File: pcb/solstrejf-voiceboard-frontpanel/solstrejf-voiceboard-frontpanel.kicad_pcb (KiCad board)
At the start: 2 copper layers, 41.1 x 123.4 mm, 14 parts, among them J1 Conn_02x08_Odd_Even, SW1 TRIG

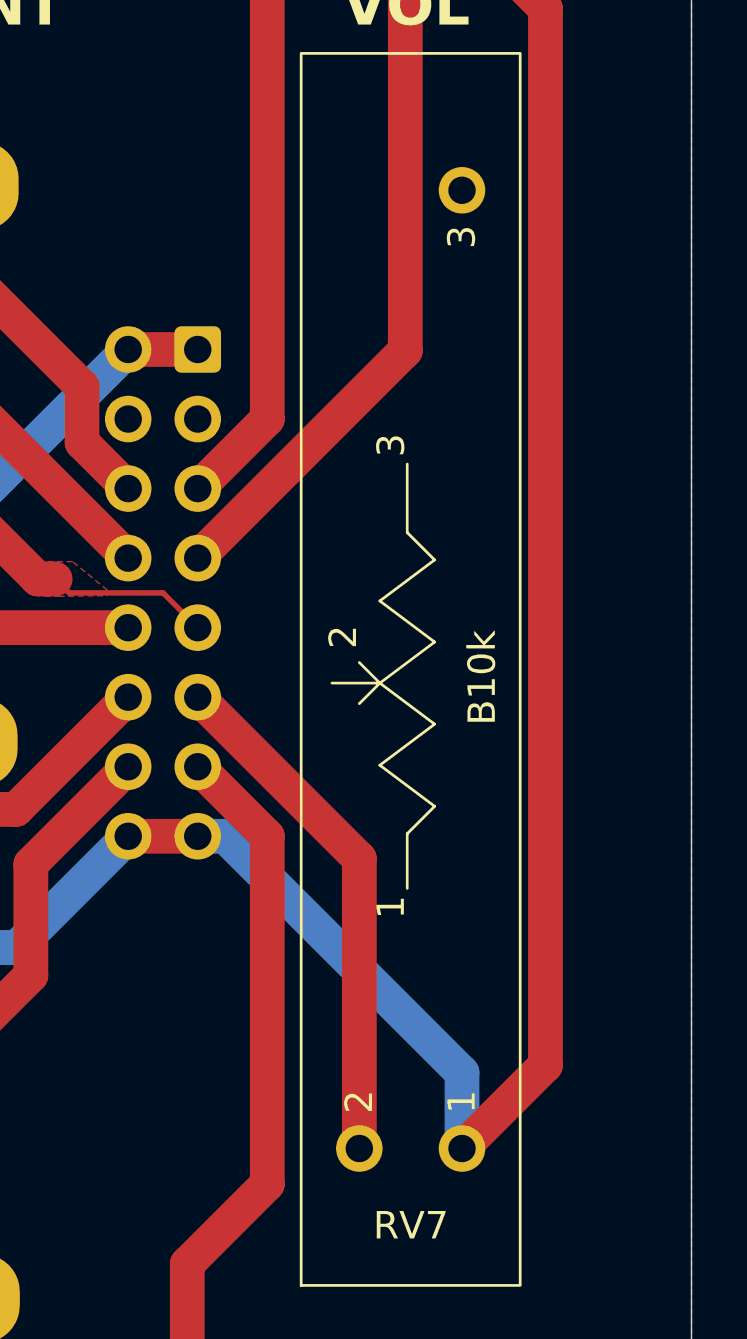
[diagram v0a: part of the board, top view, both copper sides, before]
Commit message: updated Alpha slide pot footprint to have 1.2mm drill hole diameter to match the 1mm pins
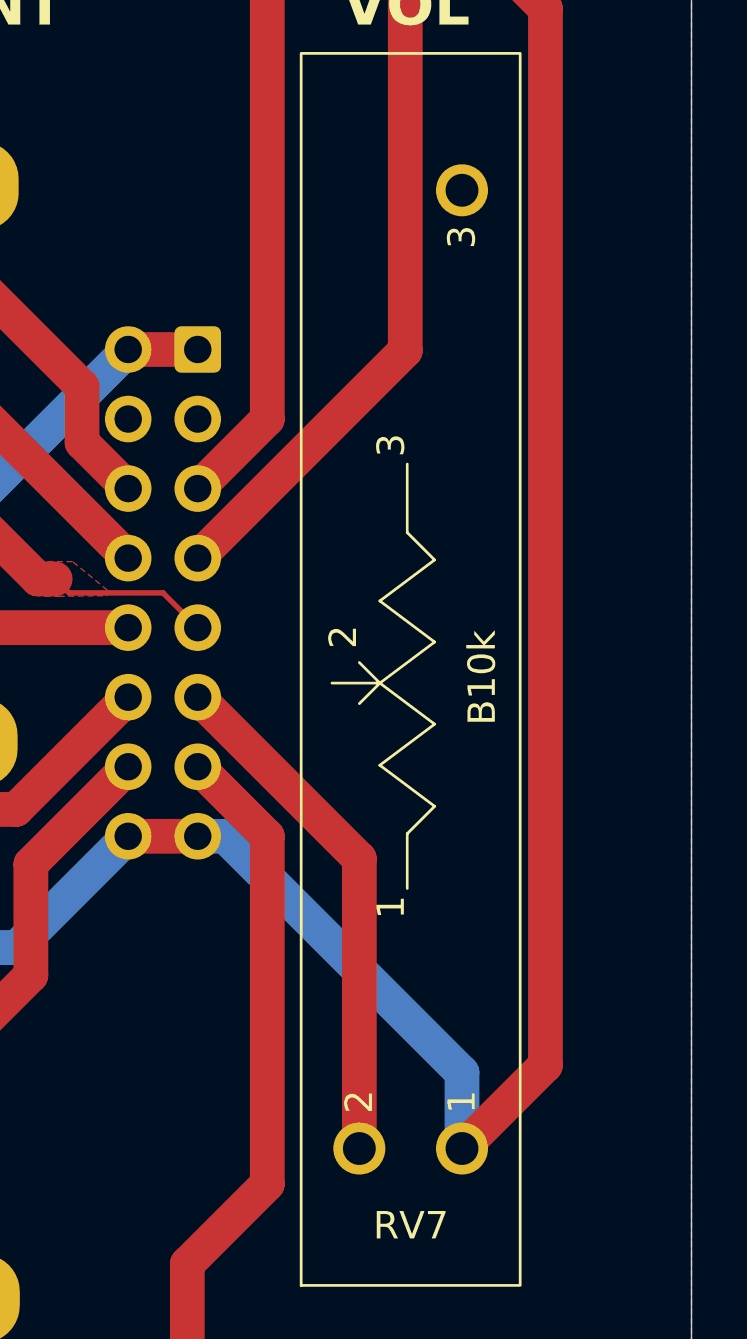
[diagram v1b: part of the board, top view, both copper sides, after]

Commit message: Added variable revision and date silkscreen prints for all four boards of Solstrejf
This means that the revision and issue date that is set in the page setup
of the PCB's will be update on the silscreen automatically so I don't forget
to update the revsions on the silkscreen :')
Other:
- board text added: "Solstrejf // Voice Board Control Panel Rev ${REVISION}"
- board text removed: "Solstrejf // Voice Board Control Panel Rev 1.0"
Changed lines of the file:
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@@
 		(layer "Edge.Cuts")
 	)
-	(gr_text "Solstrejf // Voice Board\nControl Panel Rev 1.0"
+	(gr_text "Solstrejf // Voice Board\nControl Panel Rev ${REVISION}"
 		(at 139.7 56.134 0)
 		(layer "B.SilkS")

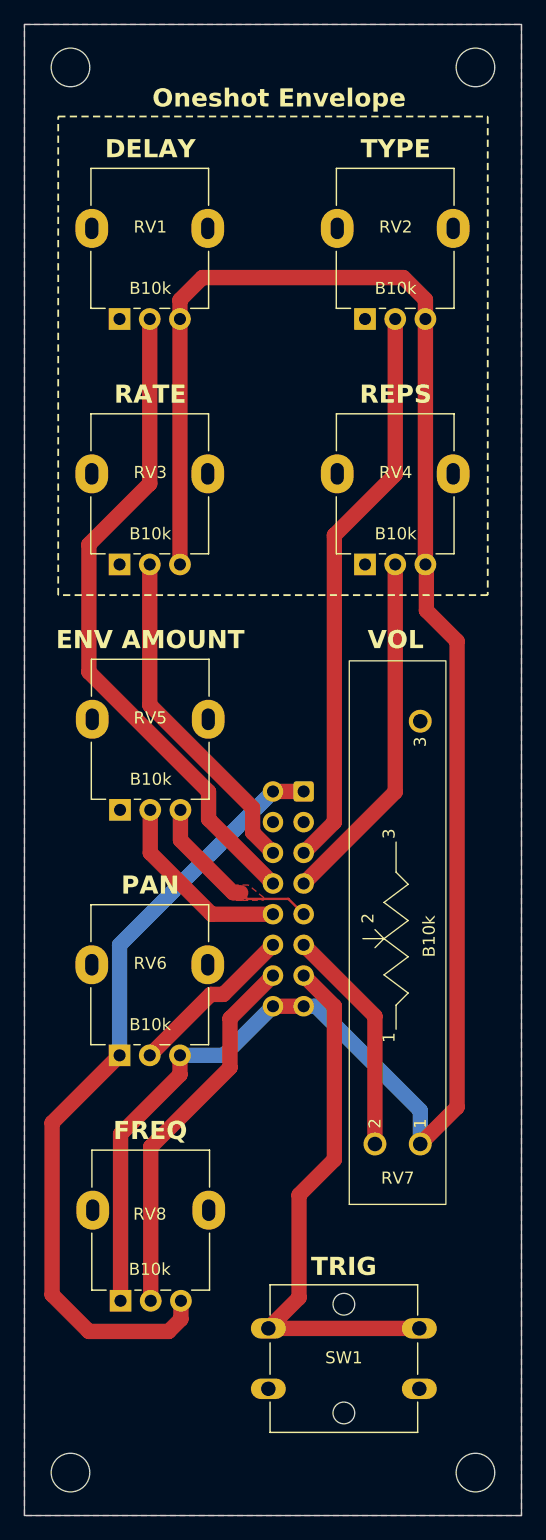
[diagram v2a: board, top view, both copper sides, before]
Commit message: updated frontpanel to rev2
- added a external trigger input for PIR motion sensor
- added a 0-5V 1V/oct cv input to the frequency cv
- PCB DRC clean
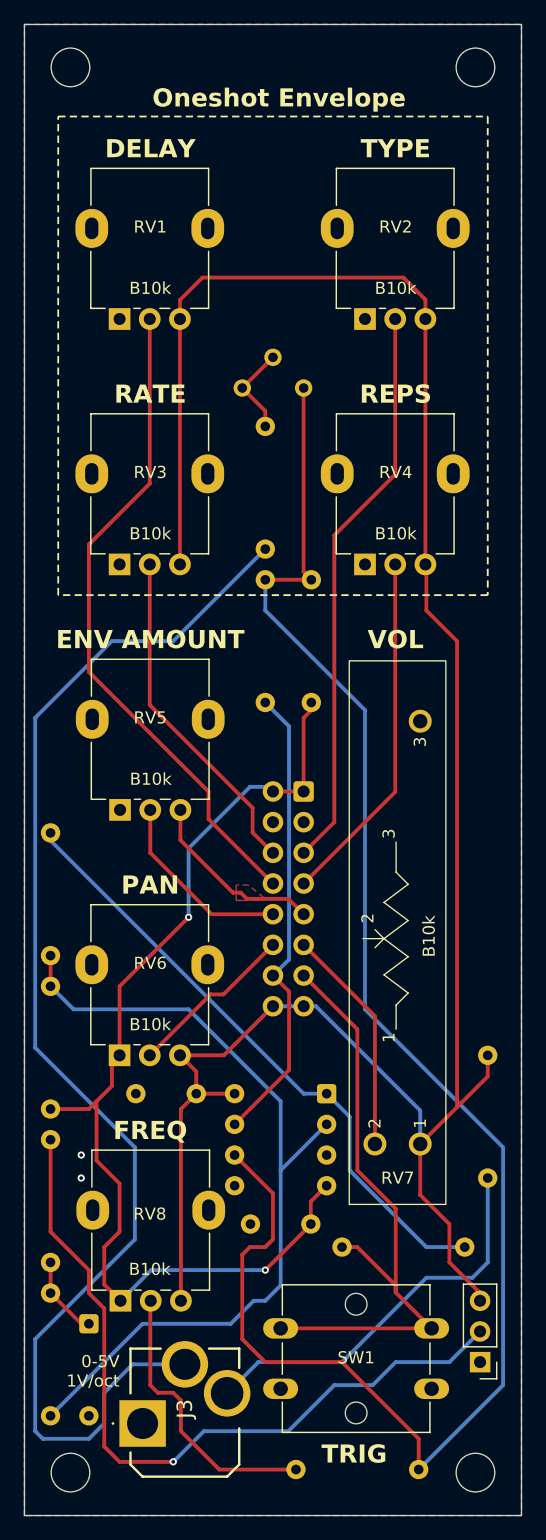
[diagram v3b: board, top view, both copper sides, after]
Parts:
- added C22: 100n, Capacitor_THT:C_Disc_D5.0mm_W2.5mm_P5.00mm, B.Cu at (133.3, 132.7)
- added C23: 100n, Capacitor_THT:C_Disc_D5.0mm_W2.5mm_P5.00mm, B.Cu at (137.8, 143.5)
- added D1: 1N4148, Diode_THT:D_DO-35_SOD27_P7.62mm_Horizontal, B.Cu at (124.5, 151.8)
- added J2: PIR Connector, Connector_PinHeader_2.54mm:PinHeader_1x03_P2.54mm_Vertical, F.Cu at (156.8, 154.9)
- added J3: SJ335052B, Kromftronics_Custom:SJ335052B, F.Cu at (128.9, 160.0)
- added R1: 10k, Resistor_THT:R_Axial_DIN0207_L6.3mm_D2.5mm_P10.16mm_Horizontal, B.Cu at (155.6, 145.4)
- added R10: 100k, Resistor_THT:R_Axial_DIN0207_L6.3mm_D2.5mm_P10.16mm_Horizontal, B.Cu at (141.6, 163.8)
- added R2: 100k, Resistor_THT:R_Axial_DIN0207_L6.3mm_D2.5mm_P10.16mm_Horizontal, B.Cu at (121.3, 121.3)
- added R3: 91k, Resistor_THT:R_Axial_DIN0207_L6.3mm_D2.5mm_P10.16mm_Horizontal, B.Cu at (121.3, 149.2)
- added R4: 10k, Resistor_THT:R_Axial_DIN0207_L6.3mm_D2.5mm_P10.16mm_Horizontal, B.Cu at (121.3, 136.5)
- added R5: 100k, Resistor_THT:R_Axial_DIN0207_L6.3mm_D2.5mm_P10.16mm_Horizontal, B.Cu at (121.3, 134.0)
- added R6: 130k, Resistor_THT:R_Axial_DIN0207_L6.3mm_D2.5mm_P10.16mm_Horizontal, B.Cu at (157.5, 129.5)
- added R7: 51k, Resistor_THT:R_Axial_DIN0207_L6.3mm_D2.5mm_P10.16mm_Horizontal, B.Cu at (139.1, 87.6)
- added R8: 100k, Resistor_THT:R_Axial_DIN0207_L6.3mm_D2.5mm_P10.16mm_Horizontal, B.Cu at (139.1, 90.2)
- added R9: 240k, Resistor_THT:R_Axial_DIN0207_L6.3mm_D2.5mm_P10.16mm_Horizontal, B.Cu at (142.9, 100.3)
- added RV9: 100k, Potentiometer_THT:Potentiometer_Bourns_3296Y_Vertical, B.Cu at (142.2, 74.3)
- added U1: TL972IP, Package_DIP:DIP-8_W7.62mm_Socket, B.Cu at (144.1, 132.7)
- moved SW1 1.02 mm to (140.3, 152.1)
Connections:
- RV8 pad 1: +5V -> -5V
- RV8 pad 2: /FREQ -> /FREQ_POT
- RV8 pad 3: -5V -> +5V
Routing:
- net Net-(U1B--): track 0.00 -> 143.6 mm
- net Net-(J3-Pad2): track 0.00 -> 107.4 mm
- net Net-(U1A--): track 0.00 -> 69.7 mm
- net /PIR_TRIG: track 0.00 -> 64.0 mm, vias 0 -> 1
- net Net-(R1-Pad1): track 0.00 -> 51.5 mm
- net Net-(J3-Pad4): track 0.00 -> 33.0 mm
- net /FREQ_POT: track 0.00 -> 23.4 mm
- net +5V: track 166.3 -> 188.9 mm
- net -5V: track 65.6 -> 88.1 mm, vias 0 -> 2
- net /FREQ: track 31.1 -> 38.7 mm
- net Net-(R7-Pad2): track 0.00 -> 7.56 mm
- net /ONESHOT_TRIG: track 45.0 -> 52.4 mm
- net Net-(D1-K): track 0.00 -> 6.77 mm
- net GND: vias 0 -> 2
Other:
- board text added: "0-5V 1V/oct"
- board text added: "CV 1V/OCT SCALE"
- board text added: "GND"
- board text added: "PIR CONNECTOR"
